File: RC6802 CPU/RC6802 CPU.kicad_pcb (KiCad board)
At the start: 2 copper layers, 99.1 x 99.1 mm, 47 parts, among them J1 Expansion, J2 RC1_UI_Port, J3 BARREL_JACK, M1 Mounting, M2 Mounting, M3 Mounting, M4 Mounting, U1 WD65C02, U2 HM62256BLP-7, U3 28C256, U4 6532, U5 74LS00, U6 LM556, U7 74LS145, U8 74LS138, U9 74LS00, X1 1MHz

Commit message: CPU board layout done
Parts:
- removed JP4: ROM_CS, Pin_Headers:Pin_Header_Straight_1x03_Pitch2.54mm
- removed RN1: 4k7x8, Resistors_THT:R_Array_SIP9
- removed U9: 74LS00, Housings_DIP:DIP-14_W7.62mm_Socket
- removed X1: 1MHz, Oscillators:Oscillator_DIP-14
- added D1: HALT, LEDs:LED_D5.0mm, F.Cu at (144.8, 50.2)
- added D2: RESET, LEDs:LED_D5.0mm, F.Cu at (134.0, 50.2)
- added D3: NMI, LEDs:LED_D5.0mm, F.Cu at (123.2, 50.2)
- added D4: IRQ, LEDs:LED_D5.0mm, F.Cu at (112.4, 50.2)
- added D5: I/O, LEDs:LED_D5.0mm, F.Cu at (187.3, 50.2)
- added D6: R/W, LEDs:LED_D5.0mm, F.Cu at (176.5, 50.2)
- added D7: VMA, LEDs:LED_D5.0mm, F.Cu at (165.7, 50.2)
- added D8: E, LEDs:LED_D5.0mm, F.Cu at (154.9, 50.2)
- added J4: DECODED, Pin_Headers:Pin_Header_Straight_1x03_Pitch2.54mm, F.Cu at (141.0, 67.3)
- added Y1: 4MHz, Crystals:Crystal_HC49-U_Vertical, F.Cu at (159.4, 62.2)
- C10: value 220nF -> 100nF
- C11: value 220nF -> 33pF
- C9: value 100nF -> 33pF
- J1: value Expansion -> RC6802_Backplane
- J2: value RC1_UI_Port -> RC6802_UI_Port
- JP1: value VP_GND -> RAM_EN; footprint Pin_Headers:Pin_Header_Straight_1x02_Pitch2.54mm -> Pin_Headers:Pin_Header_Straight_1x03_Pitch2.54mm
- JP2: value DEN -> RAM_SEL; footprint Pin_Headers:Pin_Header_Straight_1x02_Pitch2.54mm -> Pin_Headers:Pin_Header_Straight_1x03_Pitch2.54mm
- JP3: value RAM_CS -> LED_EN
- R10, R5, R8, R9: value 1k -> 220; footprint Resistors_THT:R_Axial_DIN0207_L6.3mm_D2.5mm_P10.16mm_Horizontal -> Resistors_THT:R_Axial_DIN0207_L6.3mm_D2.5mm_P7.62mm_Horizontal
- R11, R12: value 47k -> 220; footprint Resistors_THT:R_Axial_DIN0207_L6.3mm_D2.5mm_P10.16mm_Horizontal -> Resistors_THT:R_Axial_DIN0207_L6.3mm_D2.5mm_P7.62mm_Horizontal
- R3: value 3.3k -> 3k3
- R4: value 1k -> 3k3
- R6, R7: value 3k3 -> 220; footprint Resistors_THT:R_Axial_DIN0207_L6.3mm_D2.5mm_P10.16mm_Horizontal -> Resistors_THT:R_Axial_DIN0207_L6.3mm_D2.5mm_P7.62mm_Horizontal
- U1: value WD65C02 -> MC6802
- U4: value 6532 -> 74LS04; footprint Housings_DIP:DIP-40_W15.24mm_Socket -> Housings_DIP:DIP-14_W7.62mm_Socket
- U5: value 74LS00 -> 74LS138; footprint Housings_DIP:DIP-14_W7.62mm_Socket -> Housings_DIP:DIP-16_W7.62mm_Socket
- U6: value LM556 -> MC6821; footprint Housings_DIP:DIP-14_W7.62mm_Socket -> Housings_DIP:DIP-40_W15.24mm_Socket
- U7: value 74LS145 -> 74LS138
- U8: value 74LS138 -> 74LS240; footprint Housings_DIP:DIP-16_W7.62mm_Socket -> Housings_DIP:DIP-20_W7.62mm_Socket
- moved C10 90.5 mm to (137.2, 141.6), turned to 90 degrees
- moved R7 89.0 mm to (179.1, 56.5), turned to 270 degrees
- moved C4 87.1 mm to (155.6, 57.1), turned to 0 degrees
- moved R8 86.4 mm to (182.9, 56.5), turned to 270 degrees
- moved R6 85.0 mm to (175.3, 56.5), turned to 270 degrees
- moved C6 83.1 mm to (111.1, 132.1), turned to 90 degrees
- moved R12 82.0 mm to (197.5, 56.5), turned to 270 degrees
- moved R5 80.9 mm to (171.4, 56.5), turned to 270 degrees
- moved R11 79.6 mm to (193.7, 56.5), turned to 270 degrees
- moved R10 74.7 mm to (189.9, 56.5), turned to 270 degrees
- moved JP3 71.5 mm to (163.8, 68.6), turned to 0 degrees
- moved R9 71.4 mm to (186.1, 56.5), turned to 270 degrees
- moved U5 45.7 mm to (129.5, 57.1)
- moved C11 41.6 mm to (156.2, 67.3)
- moved C5 40.9 mm to (141.0, 57.1), turned to 270 degrees
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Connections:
- C10 pad 1: GND -> ~RESET
- C10 pad 2: Net-(C10-Pad2) -> GND
- C11 pad 1: GND -> Net-(C11-Pad1)
- C11 pad 2: Net-(C11-Pad2) -> GND
- C9 pad 1: VCC -> GND
- C9 pad 2: GND -> Net-(C9-Pad2)
- J1 pad 19: /PHI2 -> /E
- J1 pad 20: /~RESET -> ~RESET
- J1 pad 21: /PHI0 -> (no net)
- J1 pad 22: /~IRQ -> ~SST
- J1 pad 25: /~RDY -> /~HALT
- J1 pad 26: /SYNC -> /VMA
- J1 pad 35: /DEN -> (no net)
- J1 pad 36: K0_EXT -> (no net)
- J1 pad 37: K7_EXT -> (no net)
- J1 pad 38: IO3 -> (no net)
- J1 pad 39: TAPE -> (no net)
- J2 pad 10: /PB0 -> /PB6
- J2 pad 11: /PA7 -> /D3
- J2 pad 12: /PA0 -> /PB5
- J2 pad 13: /PA6 -> /D2
- J2 pad 14: /PA1 -> /PB4
- J2 pad 15: /PA5 -> /D1
- J2 pad 16: /PA2 -> /PB3
- J2 pad 17: /PA4 -> /D0
- J2 pad 18: /PA3 -> /PB2
- J2 pad 19: (no net) -> /R/~W
- J2 pad 20: TAPE -> /PB1
- J2 pad 22: (no net) -> /PB0
- J2 pad 23: (no net) -> /IO7
- J2 pad 24: (no net) -> /PA7
- J2 pad 25: (no net) -> /IO6
- J2 pad 26: (no net) -> /PA6
- J2 pad 27: (no net) -> /IO5
- J2 pad 28: (no net) -> /PA5
- J2 pad 29: (no net) -> /IO4
- J2 pad 3: /PB4 -> /D7
- J2 pad 30: (no net) -> /PA4
- J2 pad 31: /PHI1 -> /IO3
- J2 pad 32: (no net) -> /PA3
- J2 pad 33: /~NMI -> /IO2
- J2 pad 34: /SYNC -> /PA2
- J2 pad 35: K7 -> /IO1
- J2 pad 36: (no net) -> /PA1
- J2 pad 37: RS -> /IO0
- J2 pad 38: ST -> /PA0
- J2 pad 4: /PB3 -> ~RESET
- J2 pad 5: /PB5 -> /D6
- J2 pad 6: /PB2 -> ~SST
- J2 pad 7: /PB6 -> /D5
- J2 pad 8: /PB1 -> /PB7
- J2 pad 9: /PB7 -> /D4
- JP1 pad 1: Net-(JP1-Pad1) -> VCC
- JP1 pad 2: GND -> /RE
- JP2 pad 1: GND -> ~8K6
- JP2 pad 2: /DEN -> ~RAM_CS
- JP3 pad 1: Net-(JP3-Pad1) -> GND
- JP3 pad 2: K0 -> Net-(JP3-Pad2)
- JP3 pad 3: K0_EXT -> VCC
- R1 pad 1: /~RDY -> VCC
- R1 pad 2: VCC -> ~SST
- R10 pad 1: Net-(C11-Pad2) -> Net-(D7-Pad2)
- R10 pad 2: RS -> Net-(R10-Pad2)
- R11 pad 1: GND -> Net-(D6-Pad2)
- R11 pad 2: ST -> Net-(R11-Pad2)
- R12 pad 1: GND -> Net-(D5-Pad2)
- R12 pad 2: RS -> Net-(R12-Pad2)
- R2 pad 1: /~IRQ -> VCC
- R2 pad 2: VCC -> /~HALT
- R3 pad 1: /BE -> VCC
- R3 pad 2: VCC -> /~NMI
- R4 pad 2: Net-(JP3-Pad1) -> ~RESET
- R5 pad 1: VCC -> Net-(D4-Pad2)
- R5 pad 2: K5 -> Net-(R5-Pad2)
- R6 pad 1: /~NMI -> Net-(D3-Pad2)
- R6 pad 2: VCC -> Net-(R6-Pad2)
- R7 pad 1: /~RESET -> Net-(D2-Pad2)
- R7 pad 2: VCC -> Net-(R7-Pad2)
- R8 pad 1: VCC -> Net-(D1-Pad2)
- R8 pad 2: Net-(JP4-Pad1) -> Net-(R8-Pad2)
- R9 pad 1: Net-(C10-Pad2) -> Net-(D8-Pad2)
- R9 pad 2: ST -> Net-(R9-Pad2)
- U1 pad 1: Net-(JP1-Pad1) -> GND
- U1 pad 2: /~RDY -> /~HALT
- U1 pad 3: /PHI1 -> VCC
- U1 pad 35: (no net) -> VCC
- U1 pad 36: /BE -> /RE
- U1 pad 37: /PHI0 -> (no net)
- U1 pad 38: (no net) -> Net-(C11-Pad1)
- U1 pad 39: /PHI2 -> Net-(C9-Pad2)
- U1 pad 4: /~IRQ -> ~SST
- U1 pad 40: /~RESET -> ~RESET
- U1 pad 5: (no net) -> /VMA
- U1 pad 7: /SYNC -> /E
- U2 pad 20: K0 -> ~RAM_CS
- U2 pad 22: K0 -> ~RAM_CS
- U2 pad 27: RAM_R/~W -> /R/~W
- U3 pad 20: K7 -> ~8K7
- U3 pad 22: K7 -> ~8K7
- U4 pad 1: GND -> /E
- U4 pad 10: /PA2 -> (no net)
- U4 pad 11: /PA3 -> GND
- U4 pad 12: /PA4 -> (no net)
- U4 pad 13: /PA5 -> GND
- U4 pad 14: /PA6 -> VCC
- U4 pad 2: /A5 -> Net-(U4-Pad2)
- U4 pad 3: /~A4 -> /~8K4
- U4 pad 4: /A3 -> /8K4
- U4 pad 5: /A2 -> /~8K5
- U4 pad 6: /A1 -> /8K5
- U4 pad 7: /A0 -> GND
- U4 pad 8: /PA0 -> (no net)
- U4 pad 9: /PA1 -> GND
- U5 pad 1: /A4 -> /A13
- U5 pad 10: RAM_SEL -> /~8K5
- U5 pad 11: Net-(U5-Pad11) -> /~8K4
- U5 pad 12: Net-(U5-Pad12) -> /~8K3
- U5 pad 13: Net-(U5-Pad13) -> ~8K2
- U5 pad 14: VCC -> ~8K1
- U5 pad 2: /A4 -> /A14
- U5 pad 3: /~A4 -> /A15
- U5 pad 4: Net-(U5-Pad4) -> GND
- U5 pad 5: Net-(U5-Pad4) -> Net-(U4-Pad2)
- U5 pad 6: IO3 -> /VMA
- U5 pad 7: GND -> ~8K7
- U5 pad 8: IO2 -> GND
- U5 pad 9: Net-(U5-Pad9) -> ~8K6
- U6 pad 1: /~NMI -> GND
- U6 pad 10: VCC -> /PB0
- U6 pad 11: (no net) -> /PB1
- U6 pad 12: Net-(C11-Pad2) -> /PB2
- U6 pad 13: /~RESET -> /PB3
- U6 pad 14: VCC -> /PB4
- U6 pad 2: Net-(C10-Pad2) -> /PA0
- U6 pad 3: (no net) -> /PA1
- U6 pad 4: VCC -> /PA2
- U6 pad 5: (no net) -> /PA3
- U6 pad 6: Net-(C10-Pad2) -> /PA4
- U6 pad 7: GND -> /PA5
- U6 pad 8: Net-(C11-Pad2) -> /PA6
- U6 pad 9: (no net) -> /PA7
- U7 pad 1: Net-(JP3-Pad1) -> /A10
- U7 pad 10: (no net) -> /IO5
- U7 pad 11: (no net) -> /IO4
- U7 pad 12: /DEN -> /IO3
- U7 pad 13: /A12 -> /IO2
- U7 pad 14: /A11 -> /IO1
- U7 pad 15: /A10 -> /IO0
- U7 pad 2: Net-(JP3-Pad1) -> /A11
- U7 pad 3: Net-(JP3-Pad1) -> /A12
- U7 pad 4: Net-(JP3-Pad1) -> GND
- U7 pad 5: Net-(JP3-Pad1) -> ~8K1
- U7 pad 6: K5 -> VCC
- U7 pad 7: Net-(JP4-Pad1) -> /IO7
- U7 pad 9: Net-(JP4-Pad1) -> /IO6
- U8 pad 1: /A6 -> Net-(JP3-Pad2)
- U8 pad 10: Net-(U5-Pad9) -> GND
- U8 pad 11: Net-(U5-Pad4) -> ~8K1
- U8 pad 12: (no net) -> Net-(R5-Pad2)
- U8 pad 13: (no net) -> /R/~W
- U8 pad 14: (no net) -> Net-(R6-Pad2)
- U8 pad 15: (no net) -> /VMA
- U8 pad 16: VCC -> Net-(R7-Pad2)
- U8 pad 2: /A7 -> /~HALT
- U8 pad 3: /A8 -> Net-(R9-Pad2)
- U8 pad 4: K5 -> ~RESET
- U8 pad 5: GND -> Net-(R10-Pad2)
- U8 pad 6: /A9 -> /~NMI
- U8 pad 7: Net-(U5-Pad13) -> Net-(R11-Pad2)
- U8 pad 8: GND -> ~SST
- U8 pad 9: Net-(U5-Pad12) -> Net-(R12-Pad2)
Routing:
- net ~RESET: track 0.00 -> 194.6 mm, vias 0 -> 7
- net IO3: track 192.8 -> 0.00 mm, vias 10 -> 0
- net K7: track 184.6 -> 0.00 mm, vias 10 -> 0
- net /E: track 0.00 -> 175.7 mm, vias 0 -> 8
- net ~SST: track 0.00 -> 172.4 mm, vias 0 -> 6
- net /PHI2: track 153.2 -> 0.00 mm, vias 2 -> 0
- net /~HALT: track 0.00 -> 147.4 mm, vias 0 -> 8
- net VCC: track 494.5 -> 633.9 mm, vias 9 -> 16
- net /VMA: track 0.00 -> 136.7 mm, vias 0 -> 4
- net /~RESET: track 122.7 -> 0.00 mm, vias 6 -> 0
- net /DEN: track 119.9 -> 0.00 mm, vias 2 -> 0
- net /PHI0: track 119.6 -> 0.00 mm, vias 6 -> 0
- net Net-(JP3-Pad1): track 113.1 -> 0.00 mm, vias 8 -> 0
- net ~8K7: track 0.00 -> 107.1 mm, vias 0 -> 1
- net RAM_SEL: track 102.2 -> 0.00 mm, vias 6 -> 0
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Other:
- board text added: "$0000 - $007F"
- board text added: "$0000 - $1FFF"
- board text added: "$2000 $3FFF"
- board text added: "$4000 $4001"
- board text added: "$4000 - $5FFF"
- board text added: "$4002 $4003"
- board text added: "$C000 - $DFFF"
- board text added: "$E000 - $FFFF"
- board text added: "1-2 1-2"
- board text added: "2-3 2-3"
- board text added: "6802 CPU"
- board text added: "6821 PIA"
- board text added: "ADDRESS DECODER"
- board text added: "DATA CONTROL"
- board text added: "EEPROM"
- board text added: "EEPROM WINDOW"
- board text added: "HEX INVERTER"
- board text added: "I/O DECODER"
- board text added: "LED ENABLE"
- board text added: "LED SIGNAL BUFFER"
- board text added: "On-Chip RAM"
- board text added: "PORT A"
- board text added: "PORT B"
- board text added: "RAM_EN"
- board text added: "RAM_EN RAM_SEL"
- board text added: "RAM_SEL"
- board text added: "RC6802 Microchicken"
- board text added: "STATIC RAM"
- board text removed: "RAM_EXT"
- board text removed: "RC-ONE"
- board text removed: "ROM"
- board text removed: "ROM_EXT"

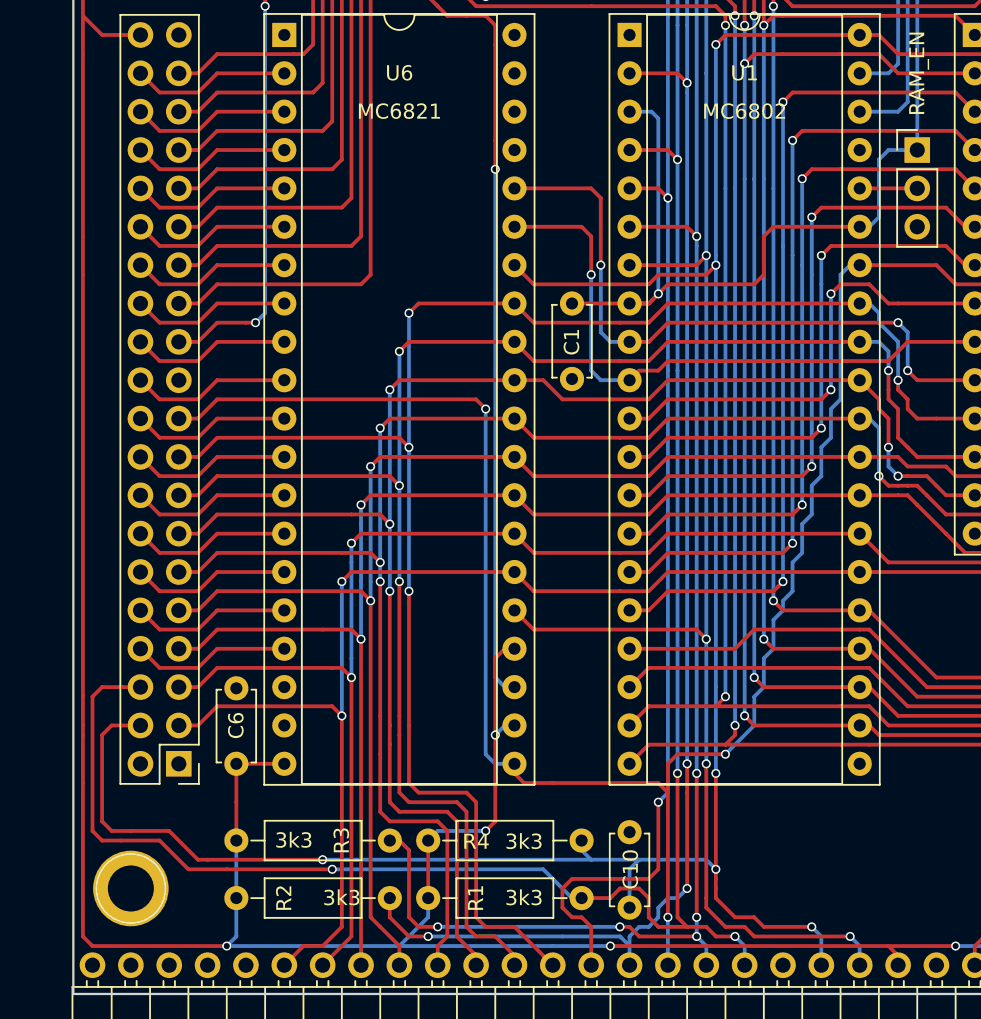
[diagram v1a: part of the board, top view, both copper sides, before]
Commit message: UI board layout done
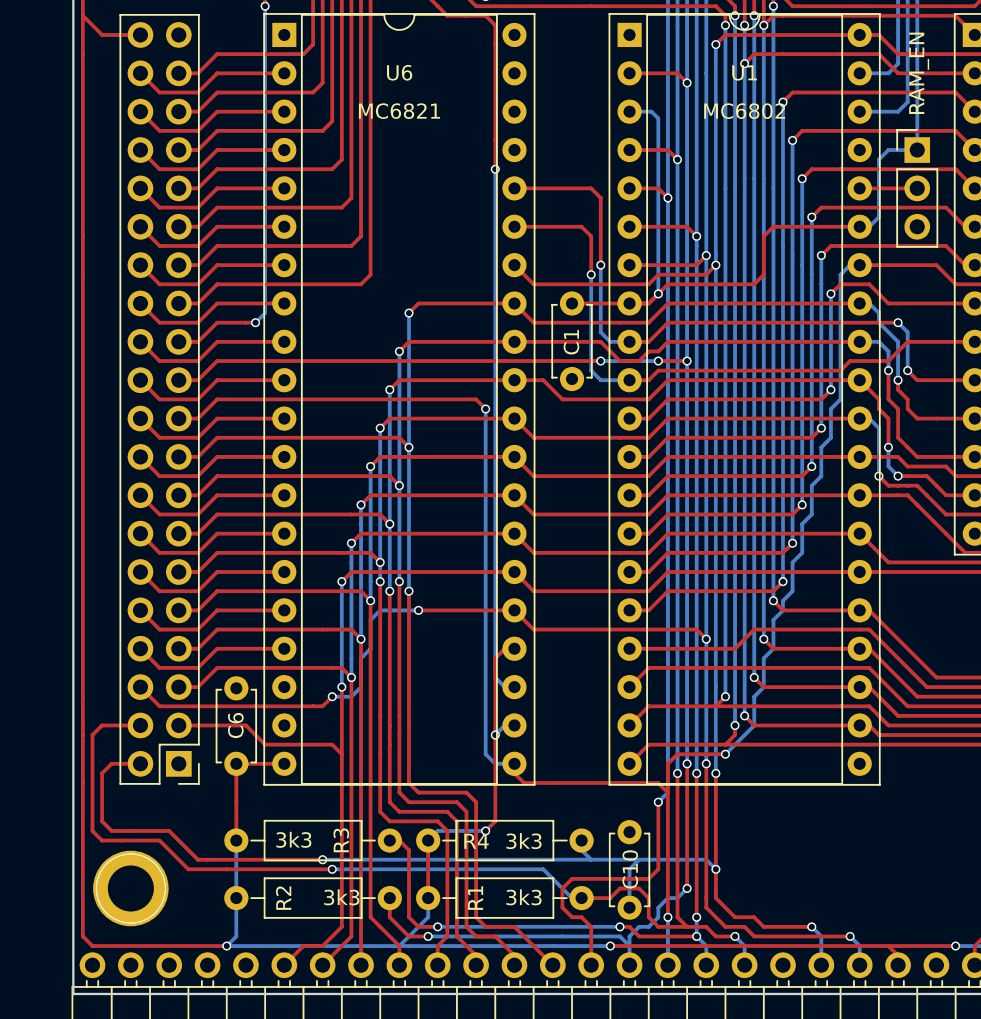
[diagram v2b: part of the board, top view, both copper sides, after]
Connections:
- net /IO0 renamed /~IO0
- net /IO1 renamed /~IO1
- net /IO2 renamed /~IO2
- net /IO3 renamed /~IO3
- net /IO4 renamed /~IO4
- net /IO5 renamed /~IO5
- net /IO6 renamed /~IO6
- net /IO7 renamed /~IO7
- J2 pad 2: GND -> ~RESET
- J2 pad 21: (no net) -> /~HALT
- J2 pad 4: ~RESET -> ~SST
- J2 pad 6: ~SST -> /E
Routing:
- net /~HALT: track 147.4 -> 181.6 mm, vias 8 -> 11
- net /E: track 175.7 -> 205.8 mm, vias 8 -> 10
- net ~RESET: track 194.6 -> 191.4 mm
- net ~SST: track 172.4 -> 169.9 mm

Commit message: Added /VMA to backplane
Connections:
- J1 pad 21: (no net) -> ~8K1
- J1 pad 26: /VMA -> /~VMA
- U4 pad 1: /E -> /VMA
- U4 pad 2: Net-(U4-Pad2) -> /~VMA
- U5 pad 5: Net-(U4-Pad2) -> /~VMA
- U5 pad 6: /VMA -> /E
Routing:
- net /~VMA: track 0.00 -> 125.5 mm, vias 0 -> 4
- net ~8K1: track 83.4 -> 171.5 mm, vias 3 -> 11
- net /VMA: track 136.7 -> 94.4 mm
- net Net-(U4-Pad2): track 21.0 -> 0.00 mm
- net /E: track 205.8 -> 203.2 mm, vias 10 -> 11
- net /D1: track 131.3 -> 130.1 mm
- net ~8K2: track 78.9 -> 79.8 mm
- net /D5: track 136.1 -> 136.8 mm
- net ~SST: track 169.9 -> 169.4 mm
- net /~NMI: track 146.2 -> 145.7 mm
- net /~HALT: track 181.6 -> 181.0 mm
- net VCC: track 633.9 -> 633.8 mm, vias 16 -> 17
- net /D2: vias 5 -> 4

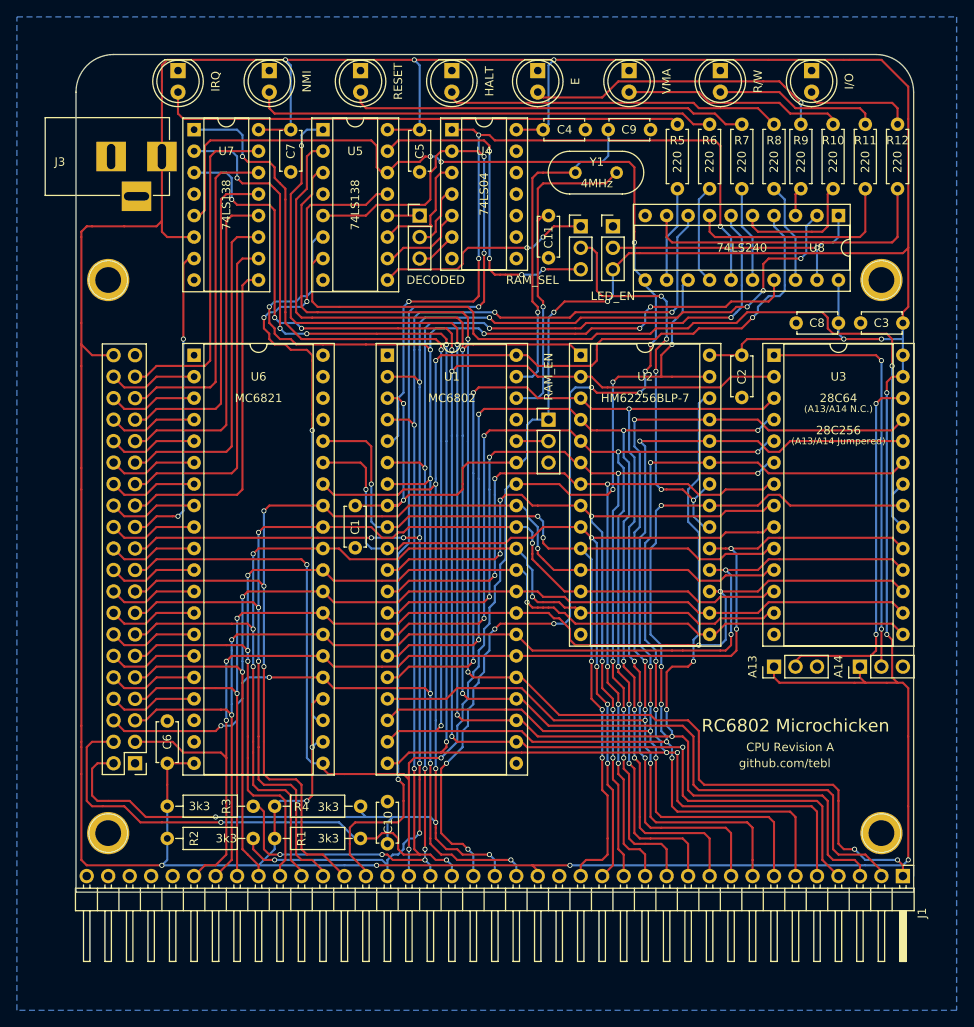
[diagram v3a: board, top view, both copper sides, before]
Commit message: Added VMA_E signal to backplane
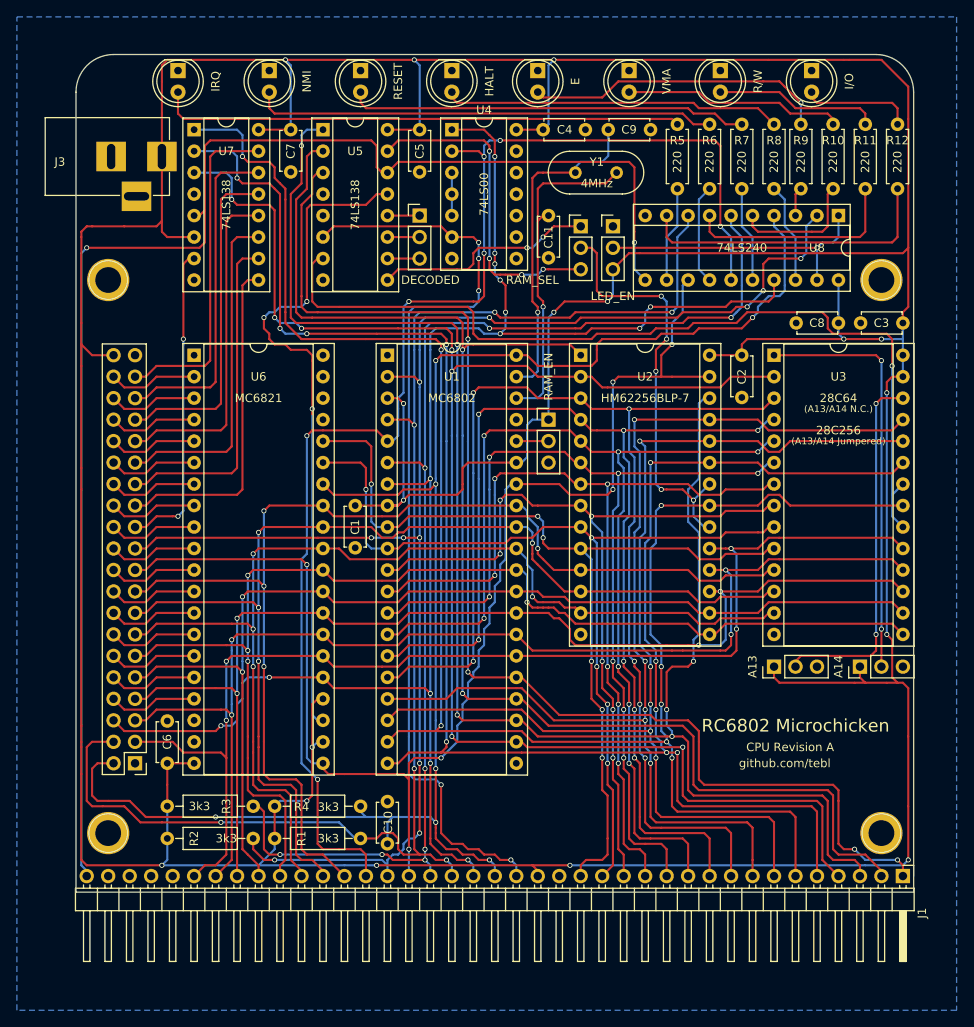
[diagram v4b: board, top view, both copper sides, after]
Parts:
- U4: value 74LS04 -> 74LS00
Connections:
- J1 pad 19: /E -> /VMA_E
- J1 pad 21: ~8K1 -> /E
- J1 pad 26: /~VMA -> /VMA
- J1 pad 39: (no net) -> ~8K1
- J4 pad 2: /8K4 -> /~8K4
- J4 pad 3: /8K5 -> /~8K5
- U4 pad 1: /VMA -> /E
- U4 pad 10: (no net) -> GND
- U4 pad 11: GND -> (no net)
- U4 pad 12: (no net) -> GND
- U4 pad 2: /~VMA -> /VMA
- U4 pad 3: /~8K4 -> Net-(U4-Pad3)
- U4 pad 4: /8K4 -> Net-(U4-Pad3)
- U4 pad 5: /~8K5 -> Net-(U4-Pad3)
- U4 pad 6: /8K5 -> /VMA_E
- U5 pad 5: /~VMA -> GND
- U5 pad 6: /E -> /VMA_E
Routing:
- net /~VMA: track 125.5 -> 0.00 mm, vias 4 -> 0
- net /VMA_E: track 0.00 -> 111.9 mm, vias 0 -> 5
- net /VMA: track 94.4 -> 162.8 mm, vias 4 -> 7
- net /E: track 203.2 -> 191.6 mm, vias 11 -> 14
- net /~8K4: track 14.0 -> 3.81 mm
- net /8K4: track 7.77 -> 0.00 mm
- net /~8K5: track 10.5 -> 3.81 mm
- net Net-(U4-Pad3): track 0.00 -> 5.08 mm
- net /8K5: track 4.86 -> 0.00 mm
- net ~8K2: track 79.8 -> 81.1 mm
- net ~8K1: track 171.5 -> 170.8 mm, vias 11 -> 2
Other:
- board text added: "NAND GATES"
- board text removed: "HEX INVERTER"
